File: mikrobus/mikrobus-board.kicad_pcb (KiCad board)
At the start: 2 copper layers, 7 parts, among them J1 Conn_01x04, P3 microBus_1, P4 microBus_2, P5 microBus_1, P6 microBus_2

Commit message: update connector
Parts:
- J1: value Conn_01x04 -> Conn_01x06; footprint Pin_Headers:Pin_Header_Straight_1x04_Pitch2.54mm -> Pin_Headers:Pin_Header_Straight_1x06_Pitch2.54mm
- moved J1 1.80 mm to (172.7, 137.2)
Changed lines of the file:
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@@
 (kicad_pcb (version 4) (host pcbnew 4.0.7)
   (general
-    (links 36)
-    (no_connects 36)
+    (links 38)
+    (no_connects 38)
     (area 0 0 0 0)
     (thickness 1.6)
@@
     (pad_to_mask_clearance 0)
     (aux_axis_origin 0 0)
-    (visible_elements FFFFFF7F)
+    (visible_elements 7FFFFFFF)
     (pcbplotparams
       (layerselection 0x00030_80000001)
@@
     (add_net "Net-(UPDUINO2_DOWN1-Pad7)")
   )
-  (module Pin_Headers:Pin_Header_Straight_1x04_Pitch2.54mm (layer F.Cu)
-    (at 171.45 138.43)
-    (descr "Through hole straight pin header, 1x04, 2.54mm pitch, single row")
-    (tags "Through hole pin header THT 1x04 2.54mm single row")
-    (fp_text reference J1 (at 0 -2.33) (layer F.SilkS)
-      (effects (font (size 1 1) (thickness 0.15)))
-    )
-    (fp_text value Conn_01x04 (at 0 9.95) (layer F.Fab)
-      (effects (font (size 1 1) (thickness 0.15)))
-    )
-    (fp_line (start -0.635 -1.27) (end 1.27 -1.27) (layer F.Fab) (width 0.1))
-    (fp_line (start 1.27 -1.27) (end 1.27 8.89) (layer F.Fab) (width 0.1))
-    (fp_line (start 1.27 8.89) (end -1.27 8.89) (layer F.Fab) (width 0.1))
-    (fp_line (start -1.27 8.89) (end -1.27 -0.635) (layer F.Fab) (width 0.1))
-    (fp_line (start -1.27 -0.635) (end -0.635 -1.27) (layer F.Fab) (width 0.1))
-    (fp_line (start -1.33 8.95) (end 1.33 8.95) (layer F.SilkS) (width 0.12))
-    (fp_line (start -1.33 1.27) (end -1.33 8.95) (layer F.SilkS) (width 0.12))
-    (fp_line (start 1.33 1.27) (end 1.33 8.95) (layer F.SilkS) (width 0.12))
-    (fp_line (start -1.33 1.27) (end 1.33 1.27) (layer F.SilkS) (width 0.12))
-    (fp_line (start -1.33 0) (end -1.33 -1.33) (layer F.SilkS) (width 0.12))
-    (fp_line (start -1.33 -1.33) (end 0 -1.33) (layer F.SilkS) (width 0.12))
-    (fp_line (start -1.8 -1.8) (end -1.8 9.4) (layer F.CrtYd) (width 0.05))
-    (fp_line (start -1.8 9.4) (end 1.8 9.4) (layer F.CrtYd) (width 0.05))
-    (fp_line (start 1.8 9.4) (end 1.8 -1.8) (layer F.CrtYd) (width 0.05))
-    (fp_line (start 1.8 -1.8) (end -1.8 -1.8) (layer F.CrtYd) (width 0.05))
-    (fp_text user %R (at 0 3.81 90) (layer F.Fab)
-      (effects (font (size 1 1) (thickness 0.15)))
-    )
-    (pad 1 thru_hole rect (at 0 0) (size 1.7 1.7) (drill 1) (layers *.Cu *.Mask)
-      (net 1 /EXT_1))
-    (pad 2 thru_hole oval (at 0 2.54) (size 1.7 1.7) (drill 1) (layers *.Cu *.Mask)
-      (net 2 /EXT_2))
-    (pad 3 thru_hole oval (at 0 5.08) (size 1.7 1.7) (drill 1) (layers *.Cu *.Mask)
-      (net 3 /EXT_3))
-    (pad 4 thru_hole oval (at 0 7.62) (size 1.7 1.7) (drill 1) (layers *.Cu *.Mask)
-      (net 4 /EXT_4))
-    (model ${KISYS3DMOD}/Pin_Headers.3dshapes/Pin_Header_Straight_1x04_Pitch2.54mm.wrl
-      (at (xyz 0 0 0))
-      (scale (xyz 1 1 1))
-      (rotate (xyz 0 0 0))
-    )
-  )
   (module Pin_Headers:Pin_Header_Straight_1x08_Pitch2.54mm (layer F.Cu)
     (at 121.92 110.49)
@@
       (at (xyz 0 0 0))
       (scale (xyz 1 1 1))
+      (rotate (xyz 0 0 0))
+    )
+  )
+  (module Pin_Headers:Pin_Header_Straight_1x06_Pitch2.54mm (layer F.Cu)
+    (at 172.72 137.16)
+    (descr "Through hole straight pin header, 1x06, 2.54mm pitch, single row")
+    (tags "Through hole pin header THT 1x06 2.54mm single row")
+    (fp_text reference J1 (at 0 -2.33) (layer F.SilkS)
+      (effects (font (size 1 1) (thickness 0.15)))
+    )
+    (fp_text value Conn_01x06 (at 0 15.03) (layer F.Fab)
+      (effects (font (size 1 1) (thickness 0.15)))
+    )
+    (fp_line (start -0.635 -1.27) (end 1.27 -1.27) (layer F.Fab) (width 0.1))
+    (fp_line (start 1.27 -1.27) (end 1.27 13.97) (layer F.Fab) (width 0.1))
+    (fp_line (start 1.27 13.97) (end -1.27 13.97) (layer F.Fab) (width 0.1))
+    (fp_line (start -1.27 13.97) (end -1.27 -0.635) (layer F.Fab) (width 0.1))
+    (fp_line (start -1.27 -0.635) (end -0.635 -1.27) (layer F.Fab) (width 0.1))
+    (fp_line (start -1.33 14.03) (end 1.33 14.03) (layer F.SilkS) (width 0.12))
+    (fp_line (start -1.33 1.27) (end -1.33 14.03) (layer F.SilkS) (width 0.12))
+    (fp_line (start 1.33 1.27) (end 1.33 14.03) (layer F.SilkS) (width 0.12))
+    (fp_line (start -1.33 1.27) (end 1.33 1.27) (layer F.SilkS) (width 0.12))
+    (fp_line (start -1.33 0) (end -1.33 -1.33) (layer F.SilkS) (width 0.12))
+    (fp_line (start -1.33 -1.33) (end 0 -1.33) (layer F.SilkS) (width 0.12))
+    (fp_line (start -1.8 -1.8) (end -1.8 14.5) (layer F.CrtYd) (width 0.05))
+    (fp_line (start -1.8 14.5) (end 1.8 14.5) (layer F.CrtYd) (width 0.05))
+    (fp_line (start 1.8 14.5) (end 1.8 -1.8) (layer F.CrtYd) (width 0.05))
+    (fp_line (start 1.8 -1.8) (end -1.8 -1.8) (layer F.CrtYd) (width 0.05))
+    (fp_text user %R (at 0 6.35 90) (layer F.Fab)
+      (effects (font (size 1 1) (thickness 0.15)))
+    )
+    (pad 1 thru_hole rect (at 0 0) (size 1.7 1.7) (drill 1) (layers *.Cu *.Mask)
+      (net 1 /EXT_1))
+    (pad 2 thru_hole oval (at 0 2.54) (size 1.7 1.7) (drill 1) (layers *.Cu *.Mask)
+      (net 2 /EXT_2))
+    (pad 3 thru_hole oval (at 0 5.08) (size 1.7 1.7) (drill 1) (layers *.Cu *.Mask)
+      (net 3 /EXT_3))
+    (pad 4 thru_hole oval (at 0 7.62) (size 1.7 1.7) (drill 1) (layers *.Cu *.Mask)
+      (net 4 /EXT_4))
+    (pad 5 thru_hole oval (at 0 10.16) (size 1.7 1.7) (drill 1) (layers *.Cu *.Mask)
+      (net 11 +3V3))
+    (pad 6 thru_hole oval (at 0 12.7) (size 1.7 1.7) (drill 1) (layers *.Cu *.Mask)
+      (net 12 GND))
+    (model ${KISYS3DMOD}/Pin_Headers.3dshapes/Pin_Header_Straight_1x06_Pitch2.54mm.wrl
+      (at (xyz 0 0 0))
+      (scale (xyz 1 1 1))

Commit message: better placing
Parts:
- moved P6 12.8 mm to (175.3, 111.8)
- moved P4 11.5 mm to (147.3, 111.8)
- moved UPDUINO2_DOWN1 7.73 mm to (127.0, 154.9)
- moved P5 5.24 mm to (152.4, 111.8)
- moved J1 3.59 mm to (175.3, 139.7)
- moved P3 2.84 mm to (124.5, 111.8)
- moved UPDUINO2_UP1 1.27 mm to (121.9, 137.2)
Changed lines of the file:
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@@
     (links 38)
     (no_connects 38)
-    (area 0 0 0 0)
+    (area 118.615 108.455 180.00762 156.845714)
     (thickness 1.6)
     (drawings 0)
@@
   )
   (module Pin_Headers:Pin_Header_Straight_1x08_Pitch2.54mm (layer F.Cu)
-    (at 121.92 110.49)
+    (at 124.46 111.76)
     (descr "Through hole straight pin header, 1x08, 2.54mm pitch, single row")
     (tags "Through hole pin header THT 1x08 2.54mm single row")
@@
   )
   (module Pin_Headers:Pin_Header_Straight_1x08_Pitch2.54mm (layer F.Cu)
-    (at 135.89 110.49)
+    (at 147.32 111.76)
     (descr "Through hole straight pin header, 1x08, 2.54mm pitch, single row")
     (tags "Through hole pin header THT 1x08 2.54mm single row")
@@
   )
   (module Pin_Headers:Pin_Header_Straight_1x08_Pitch2.54mm (layer F.Cu)
-    (at 147.32 110.49)
+    (at 152.4 111.76)
     (descr "Through hole straight pin header, 1x08, 2.54mm pitch, single row")
     (tags "Through hole pin header THT 1x08 2.54mm single row")
@@
   )
   (module Pin_Headers:Pin_Header_Straight_1x08_Pitch2.54mm (layer F.Cu)
-    (at 162.56 110.49)
+    (at 175.26 111.76)
     (descr "Through hole straight pin header, 1x08, 2.54mm pitch, single row")
     (tags "Through hole pin header THT 1x08 2.54mm single row")
@@
   )
   (module Pin_Headers:Pin_Header_Straight_1x16_Pitch2.54mm (layer F.Cu)
-    (at 125.73 147.32 90)
+    (at 127 154.94 90)
     (descr "Through hole straight pin header, 1x16, 2.54mm pitch, single row")
     (tags "Through hole pin header THT 1x16 2.54mm single row")
@@
   )
   (module Pin_Headers:Pin_Header_Straight_1x18_Pitch2.54mm (layer F.Cu)
-    (at 120.65 137.16 90)
+    (at 121.92 137.16 90)
     (descr "Through hole straight pin header, 1x18, 2.54mm pitch, single row")
     (tags "Through hole pin header THT 1x18 2.54mm single row")
@@
   )
   (module Pin_Headers:Pin_Header_Straight_1x06_Pitch2.54mm (layer F.Cu)
-    (at 172.72 137.16)
+    (at 175.26 139.7)
     (descr "Through hole straight pin header, 1x06, 2.54mm pitch, single row")
     (tags "Through hole pin header THT 1x06 2.54mm single row")

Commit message: Finished routing
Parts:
- added G1: LOGO, Graphics:mikrobus, F.Cu at (164.5, 108.0)
- added G1: LOGO, Graphics:mikrobus, F.Cu at (135.9, 108.0)
- P3, P4, P5, P6: footprint Pin_Headers:Pin_Header_Straight_1x08_Pitch2.54mm -> Socket_Strips:Socket_Strip_Straight_1x08_Pitch2.54mm
- UPDUINO2_DOWN1: footprint Pin_Headers:Pin_Header_Straight_1x16_Pitch2.54mm -> Socket_Strips:Socket_Strip_Straight_1x16_Pitch2.54mm
- UPDUINO2_UP1: footprint Pin_Headers:Pin_Header_Straight_1x18_Pitch2.54mm -> Socket_Strips:Socket_Strip_Straight_1x18_Pitch2.54mm
- moved J1 5.08 mm to (175.3, 144.8)
- moved UPDUINO2_DOWN1 5.08 mm to (127.0, 160.0)
- moved UPDUINO2_UP1 5.08 mm to (121.9, 142.2)
- moved P6 1.27 mm to (176.5, 111.8)
- moved P5 1.27 mm to (153.7, 111.8)
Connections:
- J1 pad 1: /EXT_1 -> /EXT_4
- J1 pad 2: /EXT_2 -> /EXT_3
- J1 pad 3: /EXT_3 -> /EXT_2
- J1 pad 4: /EXT_4 -> /EXT_1
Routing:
- net +3V3: track 0.00 -> 186.1 mm
- net GND: track 0.00 -> 165.3 mm
- net /AN_2: track 0.00 -> 86.4 mm
- net /RST_2: track 0.00 -> 80.8 mm
- net /PWM_2: track 0.00 -> 70.3 mm
- net /INT_2: track 0.00 -> 65.0 mm
- net /CS_2: track 0.00 -> 64.3 mm
- net /RX_2: track 0.00 -> 59.9 mm
- net /SCK_2: track 0.00 -> 59.6 mm
- net /TX_2: track 0.00 -> 56.7 mm
- net /SCL_2: track 0.00 -> 51.6 mm
- net /MISO_2: track 0.00 -> 50.7 mm
- net /EXT_1: track 0.00 -> 50.2 mm
- net /SDA_2: track 0.00 -> 46.5 mm
- net /MOSI_2: track 0.00 -> 45.3 mm
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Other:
- board outline added: 66 x 63.5 mm
- board text added: "+3.3V"
- board text added: "+5V"
- board text added: "1"
- board text added: "2"
- board text added: "AN"
- board text added: "CS"
- board text added: "GND"
- board text added: "INT"
- board text added: "MISO"
- board text added: "MOSI"
- board text added: "PWM"
- board text added: "RST"
- board text added: "RX"
- board text added: "SCK"
- board text added: "SCL"
- board text added: "SDA"
- board text added: "TX"

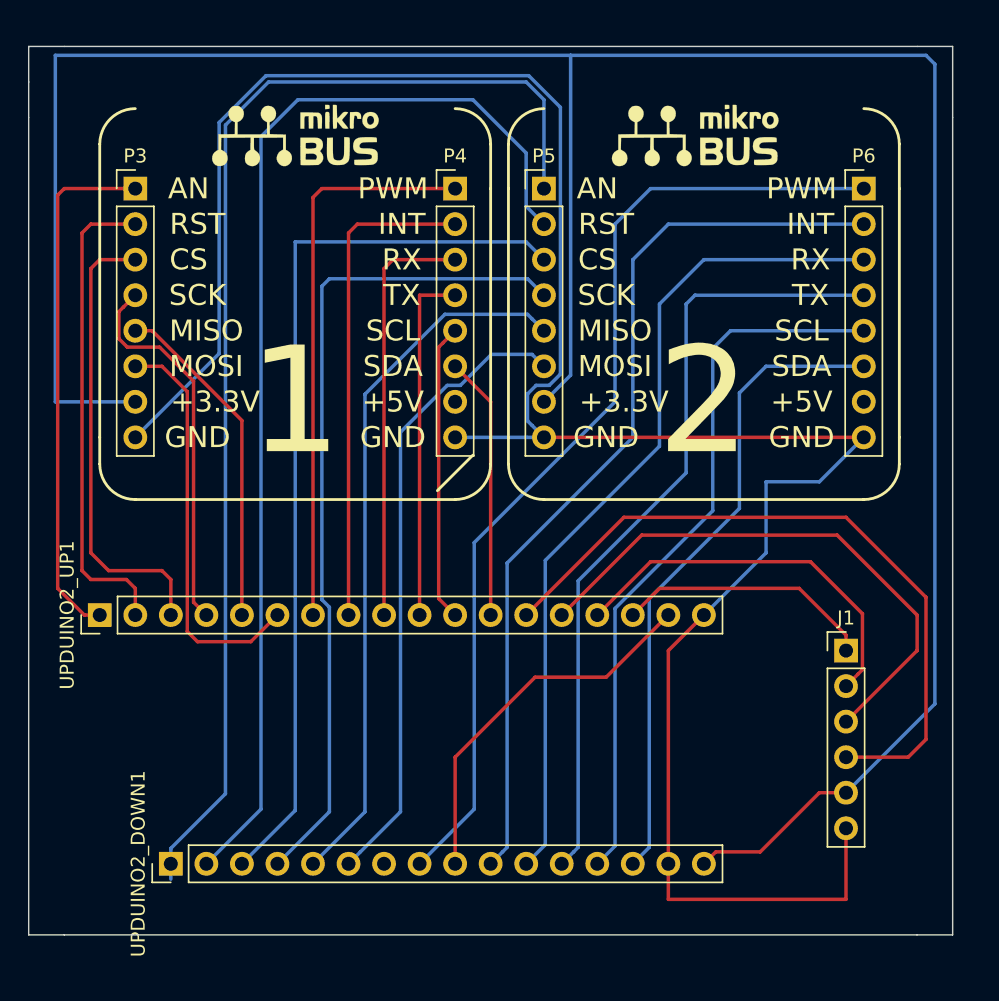
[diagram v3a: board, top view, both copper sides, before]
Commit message: Simpler routing
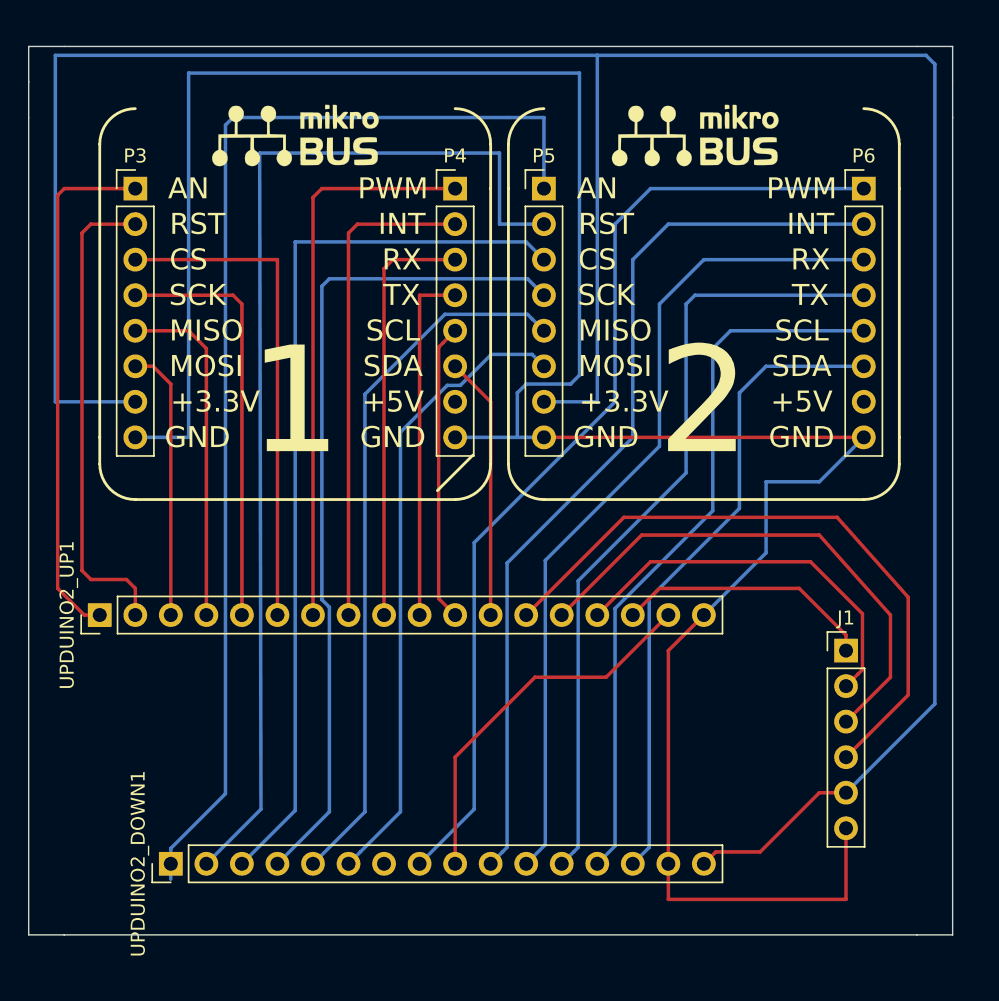
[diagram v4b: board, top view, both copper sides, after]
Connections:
- UPDUINO2_UP1 pad 3: /CS_1 -> /MOSI_1
- UPDUINO2_UP1 pad 4: /SCK_1 -> /MISO_1
- UPDUINO2_UP1 pad 5: /MISO_1 -> /SCK_1
- UPDUINO2_UP1 pad 6: /MOSI_1 -> /CS_1
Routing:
- net GND: track 165.3 -> 175.5 mm
- net /MOSI_1: track 29.1 -> 19.6 mm
- net /EXT_1: track 50.2 -> 46.0 mm
- net +3V3: track 186.1 -> 189.1 mm
- net /RST_2: track 80.8 -> 77.8 mm
- net /AN_2: track 86.4 -> 83.6 mm
- net /SCK_1: track 27.3 -> 30.1 mm
- net /CS_1: track 32.8 -> 35.6 mm
- net /EXT_2: track 39.9 -> 37.4 mm
